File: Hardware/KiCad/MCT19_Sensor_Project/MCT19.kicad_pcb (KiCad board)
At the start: 2 copper layers, 29 parts, among them J1 Sensor, J2 Vin, J3 Fan, Q1 Irf530, Q2 SI2308CDS-T1-GE3, U1 LM324, U2 L7805, U3 NodeMCU1.0(ESP-12E), U4 LM35-LP

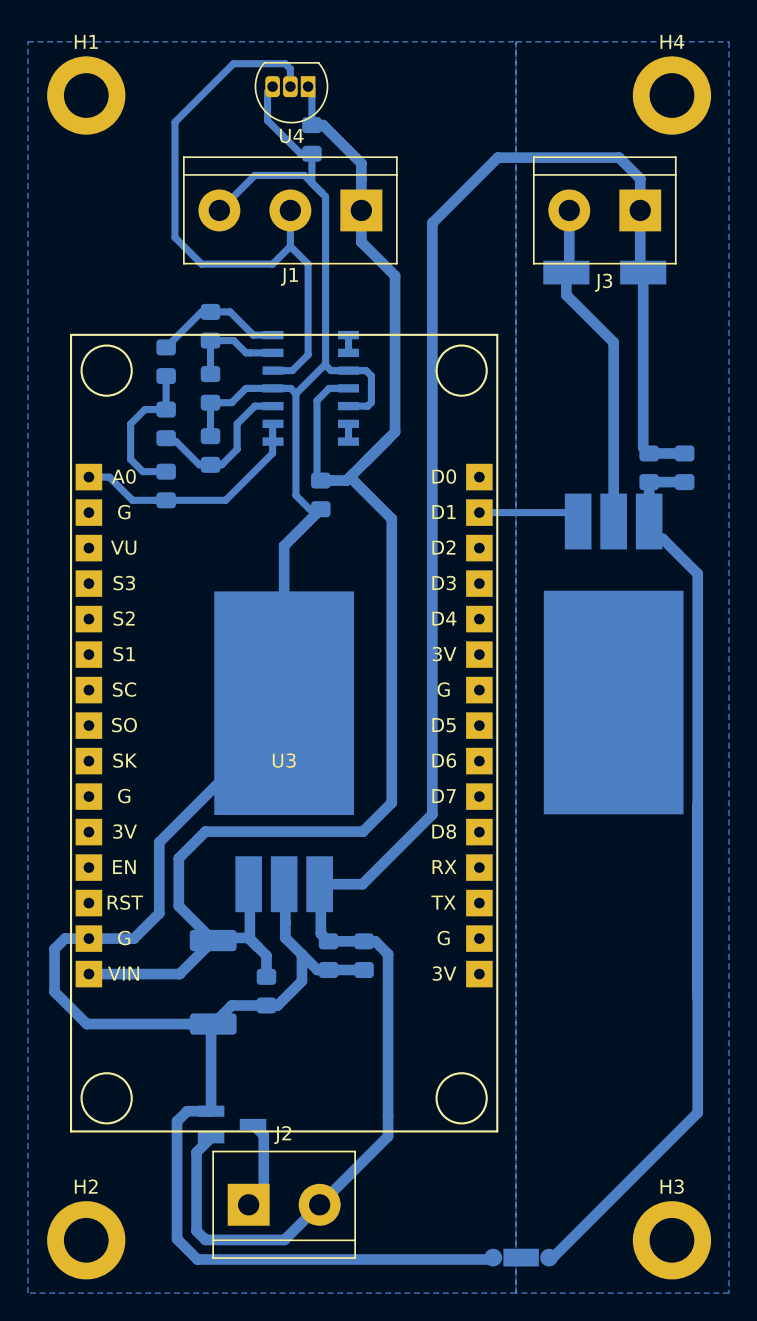
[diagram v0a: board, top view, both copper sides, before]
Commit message: Imagens do 3D e alinhamento
*hardware*
-Alinhado no layout os capacitores: C1-C2-C3-C4
-Adicionaram-se as imagens do 3D em formato png da frente e de tras
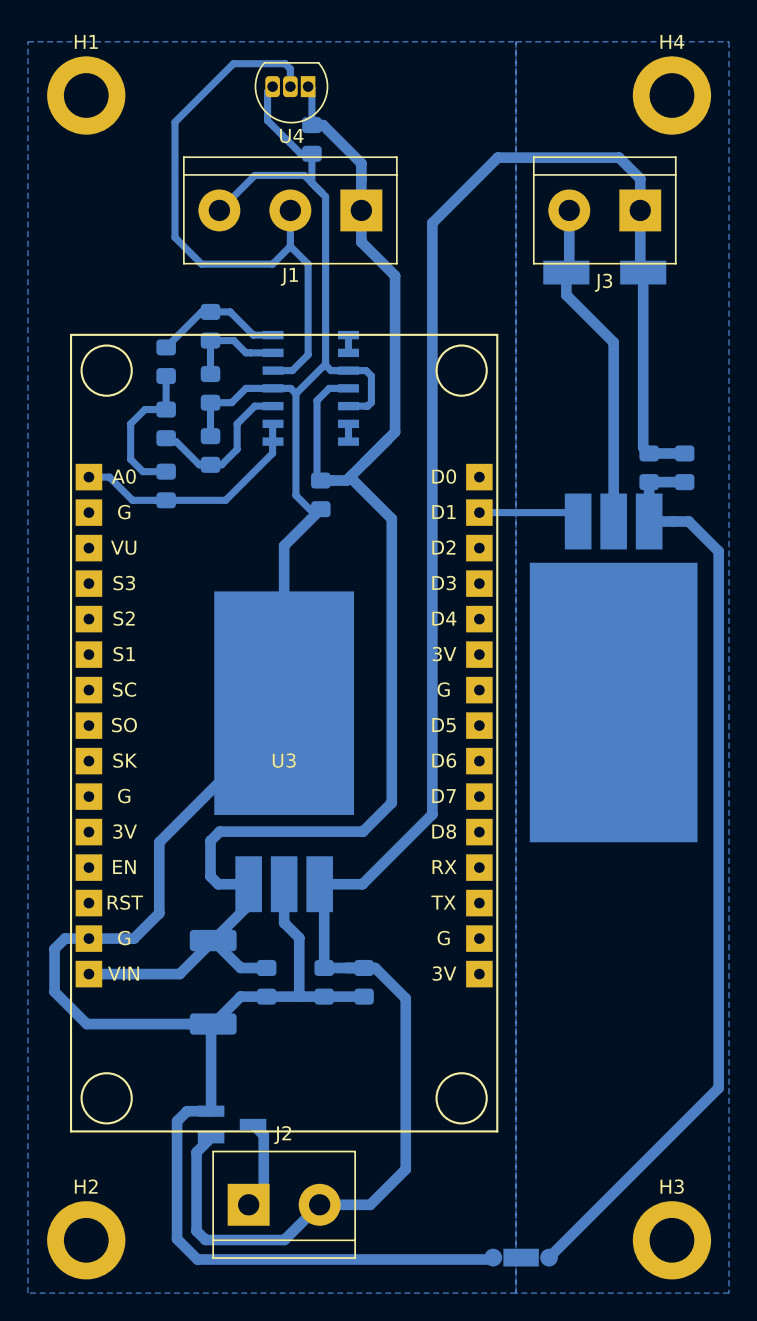
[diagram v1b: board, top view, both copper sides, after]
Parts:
- moved C2 1.93 mm to (114.2, 95.8)
- moved C1 1.91 mm to (117.0, 95.8)
- moved C3 0.64 mm to (110.1, 95.8)
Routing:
- net GND: track 78.1 -> 68.0 mm
- net VCC: track 138.5 -> 142.7 mm
- net +5V: track 116.2 -> 112.4 mm
